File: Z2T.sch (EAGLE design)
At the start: 9 parts, among them J1 M02X7-SOCKET, J2 M02X6-SOCKET

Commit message: Mechanical adjustments on Zigbee module
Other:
- note added: "Zigbee2Tasmota Zigbee Coordinator"
- note removed: "SuperHouse Automation Zigbee2Tasmota"
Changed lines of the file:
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@@
 <text x="91.44" y="68.58" size="1.778" layer="94" rot="MR0" align="bottom-right">GPIO16/!WAKE</text>
 <text x="7.62" y="6.858" size="1.778" layer="94">SKU: Z2T</text>
-<text x="7.62" y="12.7" size="2.794" layer="94">SuperHouse Automation Zigbee2Tasmota</text>
+<text x="7.62" y="12.7" size="2.794" layer="94">Zigbee2Tasmota Zigbee Coordinator</text>
 <text x="81.28" y="6.858" size="1.778" layer="94">V1.0 (2019-11-9)</text>
 <text x="32.766" y="6.858" size="1.778" layer="94">www.superhouse.tv/z2t</text>

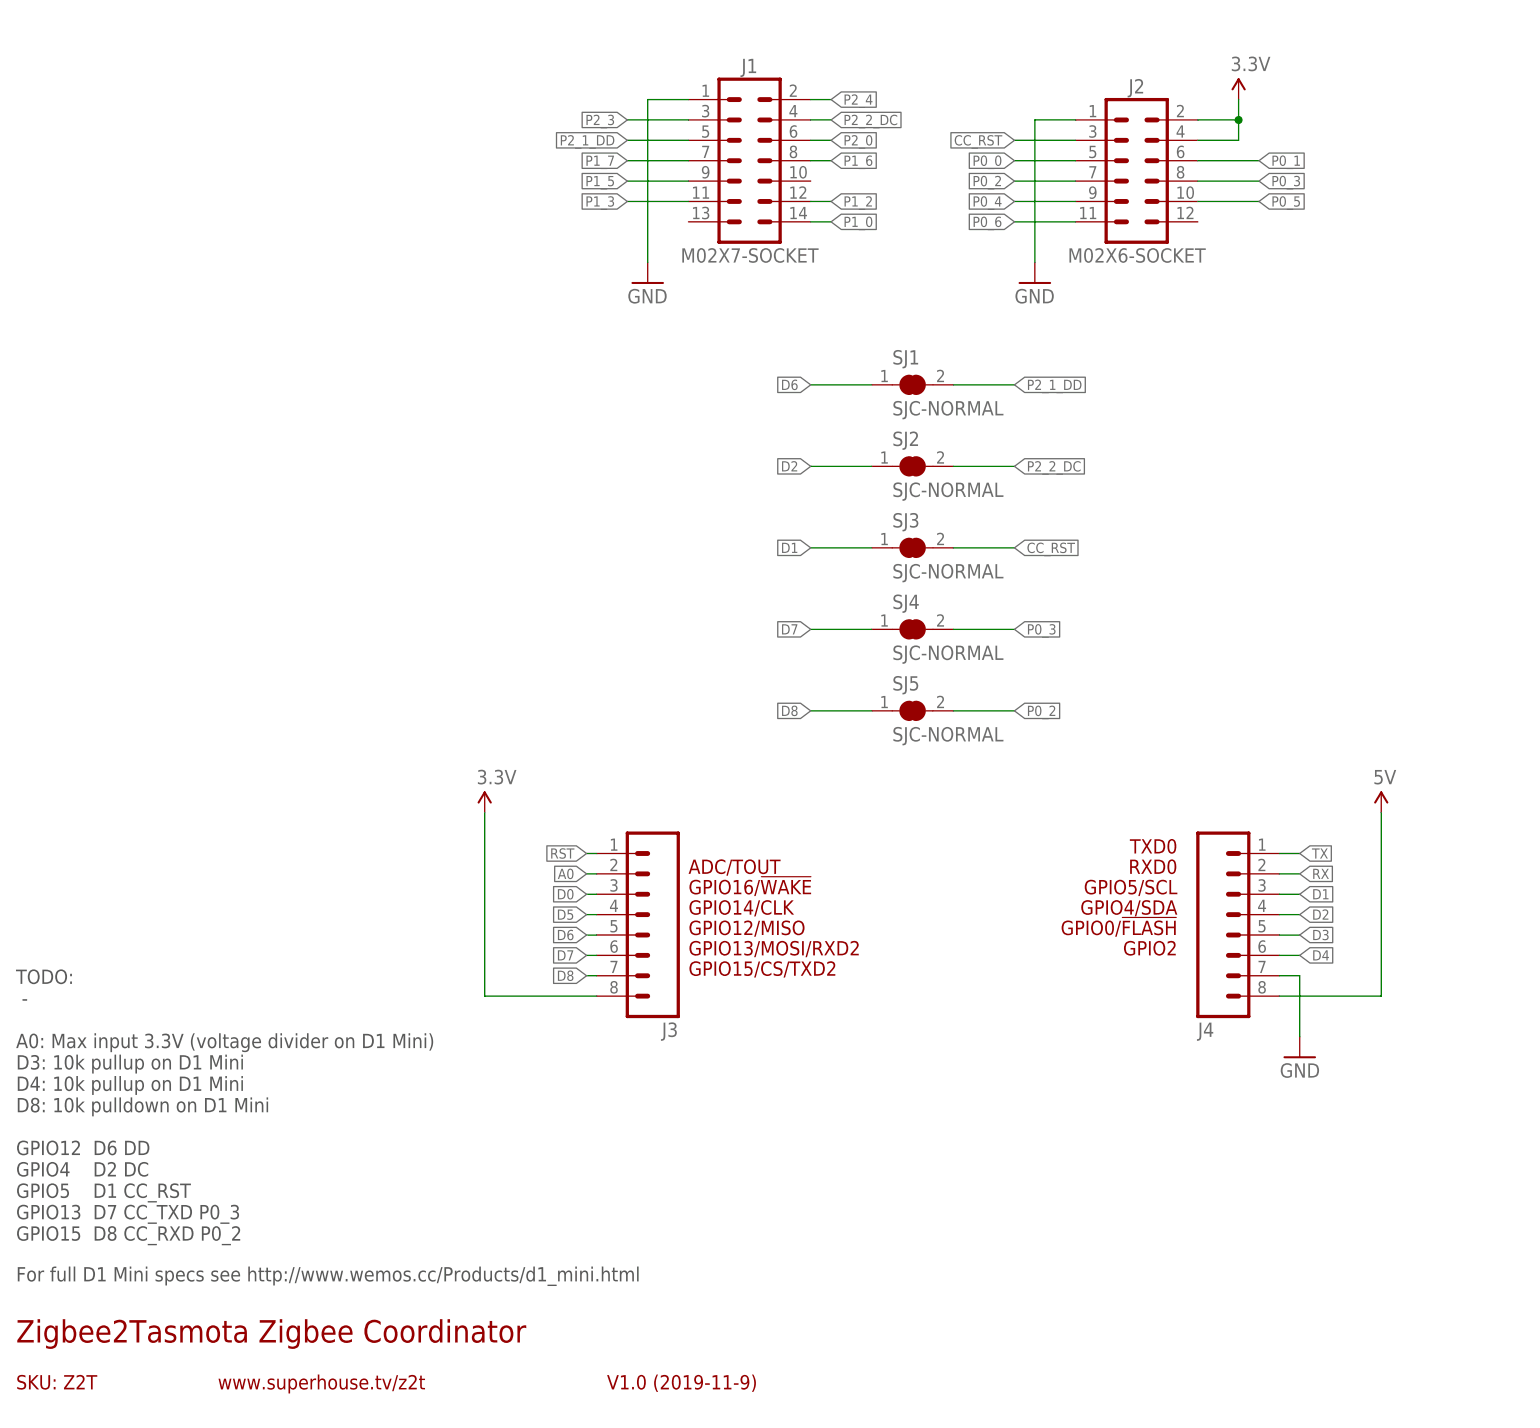
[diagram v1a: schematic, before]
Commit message: Final routing, silkscreen, DRC, and docs for v1.0 release
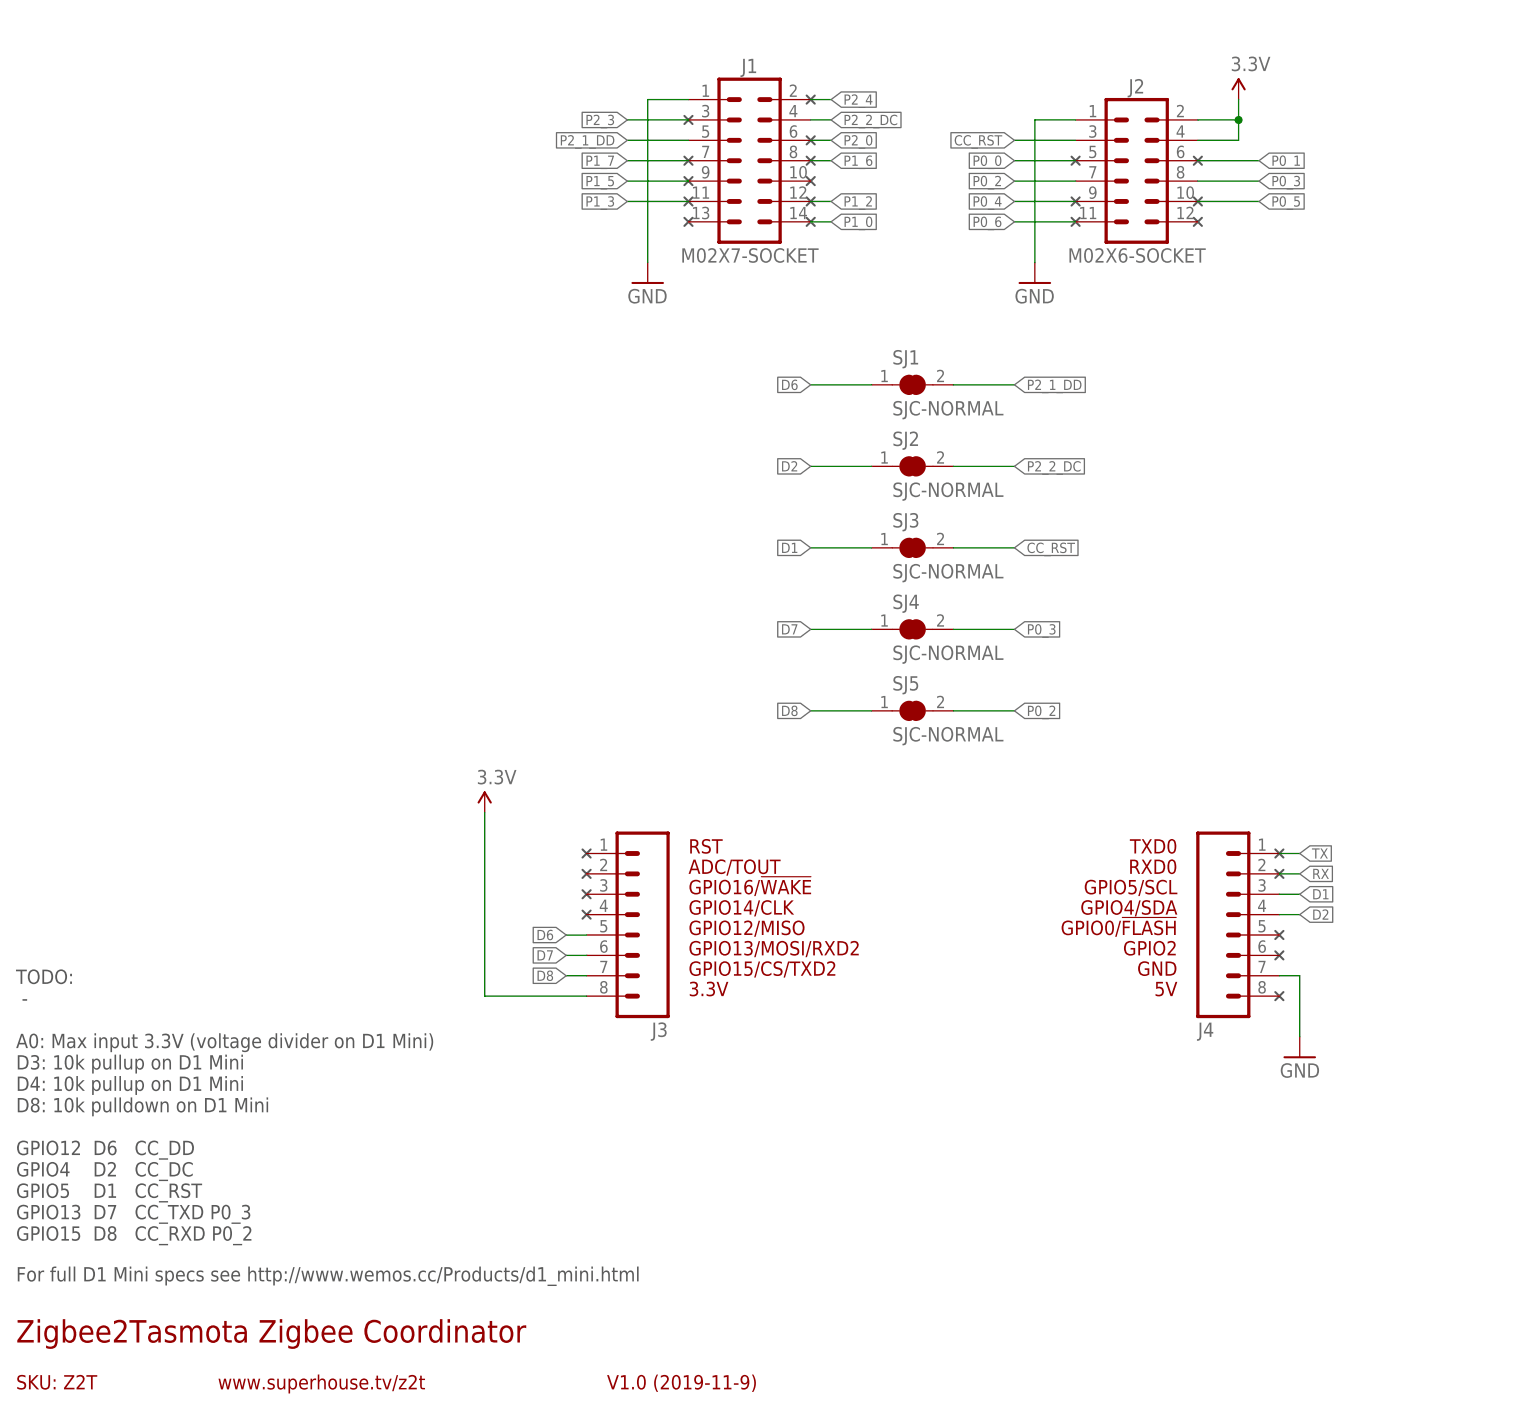
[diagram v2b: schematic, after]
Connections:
- removed net 5V: J4.8
- removed net A0: J3.2
- removed net D0: J3.3
- removed net D3: J4.5
- removed net D4: J4.6
- removed net D5: J3.4
- removed net RST: J3.1
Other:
- note added: "3.3V"
- note added: "5V"
- note added: "GND"
- note added: "RST"
- note added: "TODO: - A0: Max input 3.3V (voltage divider on D1 Mini) D3: 10k pullup on D1 Mini D4: 10k pullup on D1 Mini D8: 10k pulldown on D1 Mini GPIO12 D6 CC_DD GPIO4 D2 CC_DC GPIO5 D1 CC_RST GPIO13 D7 CC_TXD P0_3 GPIO15 D8 CC_RXD P0_2"
- note removed: "TODO: - A0: Max input 3.3V (voltage divider on D1 Mini) D3: 10k pullup on D1 Mini D4: 10k pullup on D1 Mini D8: 10k pulldown on D1 Mini GPIO12 D6 DD GPIO4 D2 DC GPIO5 D1 CC_RST GPIO13 D7 CC_TXD P0_3 GPIO15 D8 CC_RXD P0_2"
- moved on the sheet: J3

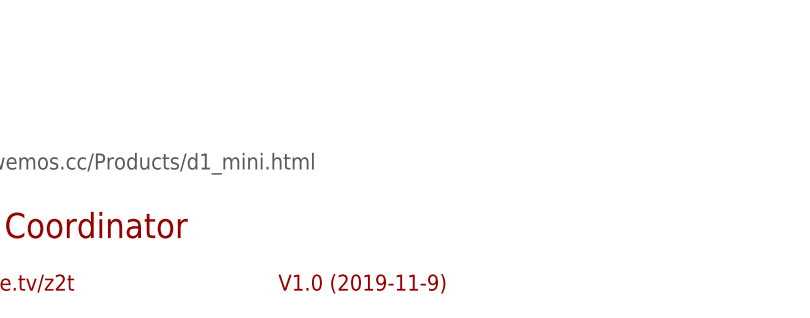
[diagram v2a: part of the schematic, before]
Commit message: Fixed spacing on Zigbee module headers
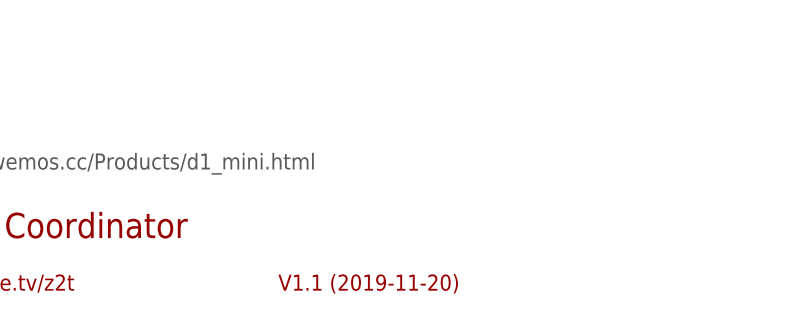
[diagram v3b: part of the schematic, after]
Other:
- note added: "V1.1 (2019-11-20)"
- note removed: "V1.0 (2019-11-9)"
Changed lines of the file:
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@@
 <text x="7.62" y="6.858" size="1.778" layer="94">SKU: Z2T</text>
 <text x="7.62" y="12.7" size="2.794" layer="94">Zigbee2Tasmota Zigbee Coordinator</text>
-<text x="81.28" y="6.858" size="1.778" layer="94">V1.0 (2019-11-9)</text>
+<text x="81.28" y="6.858" size="1.778" layer="94">V1.1 (2019-11-20)</text>
 <text x="32.766" y="6.858" size="1.778" layer="94">www.superhouse.tv/z2t</text>
 <frame x1="5.08" y1="5.08" x2="109.22" y2="17.78" columns="0" rows="0" layer="94" border-left="no" border-top="no" border-right="no" border-bottom="no"/>

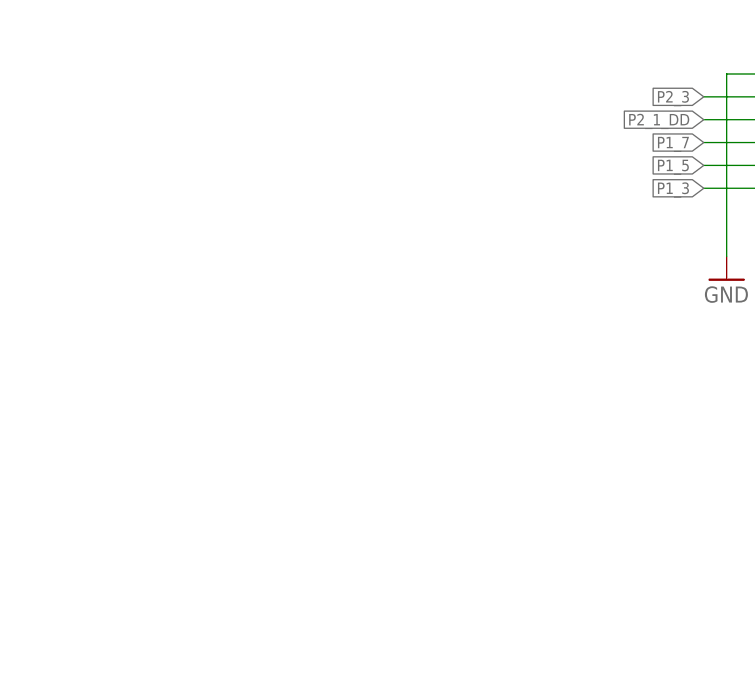
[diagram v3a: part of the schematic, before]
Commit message: Added power LED, clearance for USB socket, and pulled back copper near WiFi antenna
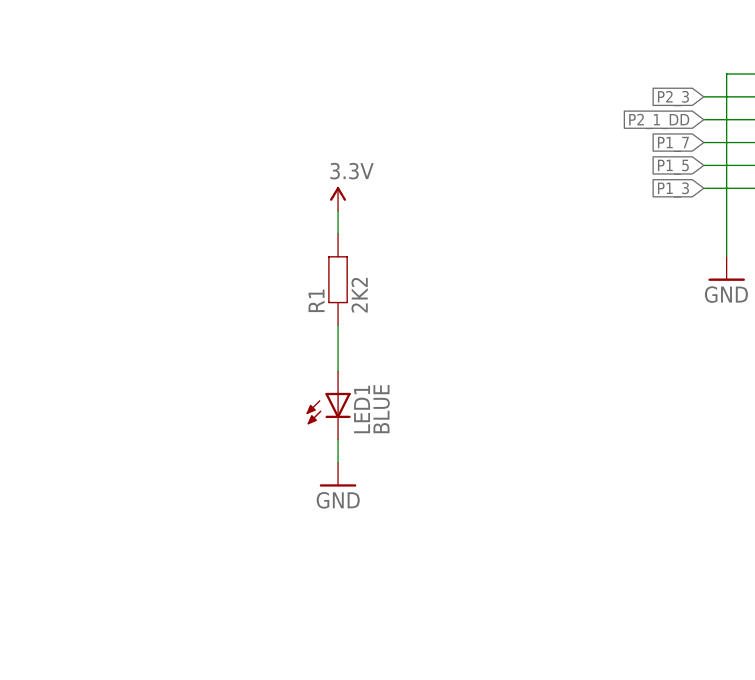
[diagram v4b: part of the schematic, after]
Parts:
- added LED1: BLUE, SuperHouse-LEDs:LED0603
- added R1: 2K2, SuperHouse-DiscreteSemi:RESISTOR0603
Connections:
- new net N$1: LED1.A, R1.1
- net 3.3V: now also R1.2
- net GND: now also LED1.C
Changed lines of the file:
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@@
 <part name="U$25" library="SuperHouse-SupplySymbols" library_urn="urn:adsk.eagle:library:11790503" deviceset="NC" device=""/>
 <part name="U$26" library="SuperHouse-SupplySymbols" library_urn="urn:adsk.eagle:library:11790503" deviceset="NC" device=""/>
+<part name="LED1" library="SuperHouse-LEDs" library_urn="urn:adsk.eagle:library:11790571" deviceset="LED" device="0603" package3d_urn="urn:adsk.eagle:package:7066240/3" value="BLUE"/>
+<part name="R1" library="SuperHouse-DiscreteSemi" library_urn="urn:adsk.eagle:library:11768461" deviceset="RESISTOR" device="0603" package3d_urn="urn:adsk.eagle:package:11768543/2" value="2K2"/>
+<part name="P+1" library="SuperHouse-SupplySymbols" library_urn="urn:adsk.eagle:library:11790503" deviceset="3.3V" device=""/>
+<part name="GND4" library="freetronics-original" deviceset="GND" device=""/>
 </parts>
 <sheets>
@@
 <instance part="U$25" gate="G$1" x="165.1" y="71.12" smashed="yes"/>
 <instance part="U$26" gate="G$1" x="106.68" y="154.94" smashed="yes"/>
+<instance part="LED1" gate="G$1" x="43.18" y="132.08" smashed="yes">
+<attribute name="NAME" x="46.736" y="127.508" size="1.778" layer="95" rot="R90"/>
+<attribute name="VALUE" x="48.895" y="127.508" size="1.778" layer="96" rot="R90"/>
+</instance>
+<instance part="R1" gate="G$1" x="43.18" y="144.78" smashed="yes" rot="R90">
+<attribute name="NAME" x="41.6814" y="140.97" size="1.778" layer="95" rot="R90"/>
+<attribute name="VALUE" x="46.482" y="140.97" size="1.778" layer="96" rot="R90"/>
+</instance>
+<instance part="P+1" gate="G$1" x="43.18" y="152.4" smashed="yes">
+<attribute name="VALUE" x="42.164" y="155.956" size="1.778" layer="96"/>
+</instance>
+<instance part="GND4" gate="1" x="43.18" y="121.92" smashed="yes" rot="MR0">
+<attribute name="VALUE" x="45.72" y="119.38" size="1.778" layer="96" rot="MR0"/>
+</instance>
 </instances>
 <busses>
@@
 <pinref part="GND3" gate="1" pin="GND"/>
 <wire x1="134.62" y1="165.1" x2="134.62" y2="147.32" width="0.1524" layer="91"/>
+</segment>
+<segment>
+<pinref part="LED1" gate="G$1" pin="C"/>
+<pinref part="GND4" gate="1" pin="GND"/>
+<wire x1="43.18" y1="127" x2="43.18" y2="124.46" width="0.1524" layer="91"/>
 </segment>
 </net>
@@
 <junction x="160.02" y="165.1"/>
 </segment>
+<segment>
+<pinref part="P+1" gate="G$1" pin="3.3V"/>
+<pinref part="R1" gate="G$1" pin="2"/>
+<wire x1="43.18" y1="152.4" x2="43.18" y2="149.86" width="0.1524" layer="91"/>
+</segment>
 </net>
 <net name="CC_RST" class="0">
@@
 <wire x1="154.94" y1="154.94" x2="162.56" y2="154.94" width="0.1524" layer="91"/>
 <label x="162.56" y="154.94" size="1.27" layer="95" xref="yes"/>
+</segment>
+</net>
+<net name="N$1" class="0">
+<segment>
+<pinref part="R1" gate="G$1" pin="1"/>
+<pinref part="LED1" gate="G$1" pin="A"/>
+<wire x1="43.18" y1="139.7" x2="43.18" y2="134.62" width="0.1524" layer="91"/>
 </segment>
 </net>
@@
 packages will not be understood (or retained) with this version.
 </note>
+<note version="8.4" severity="warning">
+Since Version 8.4, EAGLE supports properties for SPICE simulation.
+Probes in schematics and SPICE mapping objects found in parts and library devices
+will not be understood with this version. Update EAGLE to the latest version
+for full support of SPICE simulation.
+</note>
 </compatibility>
